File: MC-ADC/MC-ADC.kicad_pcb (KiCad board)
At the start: 2 copper layers, 160 x 100 mm, 6 parts, among them J1 Conn_Coaxial, J12 Conn_Coaxial, J2 Conn_Coaxial, J3 Conn_Coaxial, J4 Conn_Coaxial, J5 Conn_Coaxial

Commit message: ADC Work + Start Layout
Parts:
- removed J12, J5: Conn_Coaxial, Connector_Coaxial:BNC_Amphenol_031-6575_Horizontal
- added C10: 4.7 uF, Capacitor_SMD:C_1210_3225Metric, F.Cu at (134.4, 67.3)
- added C11: 2.2 uF, Capacitor_SMD:C_1210_3225Metric, F.Cu at (123.9, 126.7)
- added C12: unpopulated, Capacitor_SMD:C_1210_3225Metric, F.Cu at (128.1, 126.7)
- added C13: unpopulated, Capacitor_SMD:C_1210_3225Metric, F.Cu at (137.1, 126.9)
- added C14: 0.1 uF, Capacitor_SMD:C_1210_3225Metric, F.Cu at (96.3, 56.6)
- added C15: 0.1 uF, Capacitor_SMD:C_1210_3225Metric, F.Cu at (96.4, 62.4)
- added C16: 10 uF, Capacitor_SMD:C_1210_3225Metric, F.Cu at (109.4, 58.0)
- added C17: 0.1 uF, Capacitor_SMD:C_1210_3225Metric, F.Cu at (109.4, 61.6)
- added C18: unpopulated, Capacitor_SMD:C_1210_3225Metric, F.Cu at (143.1, 64.3)
- added C20: 1pF, Capacitor_SMD:C_0603_1608Metric, F.Cu at (111.2, 88.2)
- added C30: 1pF, Capacitor_SMD:C_0603_1608Metric, F.Cu at (111.0, 99.9)
- added C40: 1pF, Capacitor_SMD:C_0603_1608Metric, F.Cu at (113.5, 114.3)
- added C80: 43 nF, Capacitor_SMD:C_0805_2012Metric, F.Cu at (125.2, 83.4)
- added C81: 470 pF, Capacitor_SMD:C_1206_3216Metric, F.Cu at (125.6, 87.3)
- added C82: 470 pF, Capacitor_SMD:C_1206_3216Metric, F.Cu at (139.1, 92.2)
- added C83: 470 pF, Capacitor_SMD:C_1206_3216Metric, F.Cu at (125.6, 98.1)
- added C84: 43 nF, Capacitor_SMD:C_0805_2012Metric, F.Cu at (124.9, 101.9)
- added C85: 43 nF, Capacitor_SMD:C_0805_2012Metric, F.Cu at (138.8, 95.9)
- added D20: D_Schottky, Package_TO_SOT_SMD:SOT-23, F.Cu at (184.6, 72.1)
- added D21: D_Schottky, Package_TO_SOT_SMD:SOT-23, F.Cu at (184.6, 64.6)
- added D30: D_Schottky, Package_TO_SOT_SMD:SOT-23, F.Cu at (184.0, 100.8)
- added D31: D_Schottky, Package_TO_SOT_SMD:SOT-23, F.Cu at (184.0, 93.3)
- added D41: D_Schottky, Package_TO_SOT_SMD:SOT-23, F.Cu at (185.0, 129.0)
- added D42: D_Schottky, Package_TO_SOT_SMD:SOT-23, F.Cu at (185.0, 121.5)
- added JP1: Jumper, Connector_PinHeader_2.54mm:PinHeader_1x03_P2.54mm_Vertical, F.Cu at (207.9, 70.7)
- added JP2: Jumper, Connector_PinHeader_2.54mm:PinHeader_1x03_P2.54mm_Vertical, F.Cu at (207.6, 98.7)
- added JP3: Jumper, Connector_PinHeader_2.54mm:PinHeader_1x03_P2.54mm_Vertical, F.Cu at (207.9, 127.2)
- added L10: 3.9 uH, Inductor_SMD:L_1812_4532Metric_Pad1.30x3.40mm_HandSolder, F.Cu at (129.8, 67.2)
- added L11: 10uH, Footprints_MC-ADC:INDPM4040X190N, F.Cu at (117.7, 127.0)
- added R10: 1.87K, Resistor_SMD:R_0603_1608Metric, F.Cu at (107.0, 64.6)
- added R11: 1.43K, Resistor_SMD:R_0603_1608Metric, F.Cu at (110.6, 64.7)
- added R12: 30.9K, Resistor_SMD:R_1206_3216Metric, F.Cu at (132.7, 126.7)
- added R13: 1.07K, Resistor_SMD:R_1206_3216Metric, F.Cu at (130.4, 120.5)
- added R20: 250R, Resistor_SMD:R_0603_1608Metric, F.Cu at (108.5, 82.5)
- added R21: 1K, Resistor_SMD:R_0603_1608Metric, F.Cu at (160.6, 64.5)
- added R22: 100R, Resistor_SMD:R_0603_1608Metric, F.Cu at (160.6, 69.9)
- added R23: 1M, Resistor_SMD:R_1206_3216Metric, F.Cu at (202.2, 70.6)
- added R24: 50R, Resistor_SMD:R_0603_1608Metric, F.Cu at (202.2, 65.3)
- added R25: 10K, Resistor_SMD:R_1206_3216Metric, F.Cu at (193.2, 68.0)
- added R26: DNP, Resistor_SMD:R_1206_3216Metric, F.Cu at (204.6, 77.3)
- added R30: 250R, Resistor_SMD:R_0603_1608Metric, F.Cu at (108.9, 94.6)
- added R31: 100R, Resistor_SMD:R_0603_1608Metric, F.Cu at (159.7, 99.0)
- added R32: 1K, Resistor_SMD:R_0603_1608Metric, F.Cu at (159.6, 94.0)
- added R33: 1M, Resistor_SMD:R_1206_3216Metric, F.Cu at (202.0, 98.8)
- added R34: 50R, Resistor_SMD:R_0603_1608Metric, F.Cu at (201.9, 93.5)
- added R35: 10K, Resistor_SMD:R_1206_3216Metric, F.Cu at (192.8, 96.6)
- added R36: DNP, Resistor_SMD:R_1206_3216Metric, F.Cu at (204.4, 105.4)
- added R40: 250R, Resistor_SMD:R_0603_1608Metric, F.Cu at (111.0, 108.8)
- added R41: 100R, Resistor_SMD:R_0603_1608Metric, F.Cu at (160.2, 127.2)
- added R42: 1K, Resistor_SMD:R_0603_1608Metric, F.Cu at (160.0, 122.2)
- added R43: 1M, Resistor_SMD:R_1206_3216Metric, F.Cu at (201.9, 126.9)
- added R44: 50R, Resistor_SMD:R_0603_1608Metric, F.Cu at (201.9, 121.8)
- added R45: 10K, Resistor_SMD:R_1206_3216Metric, F.Cu at (193.2, 124.2)
- added R46: DNP, Resistor_SMD:R_1206_3216Metric, F.Cu at (204.5, 133.9)
- added R80: 2.2K, Resistor_SMD:R_1206_3216Metric, F.Cu at (131.2, 86.0)
- added R81: 330R, Resistor_SMD:R_0603_1608Metric, F.Cu at (125.7, 91.0)
- added R82: 330R, Resistor_SMD:R_0603_1608Metric, F.Cu at (138.6, 88.2)
- added R83: 330R, Resistor_SMD:R_0603_1608Metric, F.Cu at (125.6, 94.5)
- added R84: 2.2K, Resistor_SMD:R_1206_3216Metric, F.Cu at (131.2, 98.2)
- added R85: 2.2K, Resistor_SMD:R_1206_3216Metric, F.Cu at (139.3, 98.6)
- added R86: 10K, Resistor_SMD:R_1206_3216Metric, F.Cu at (80.5, 60.5)
- added U10: MAX6126AASA30+, Package_SO:SOIC-8_3.9x4.9mm_P1.27mm, F.Cu at (102.6, 59.9)
- added U11: R-78E3.3-0.5, Package_SIP:SIP3_11.6x8.5mm, F.Cu at (131.7, 60.4)
- added U12: RD-2412D_P, Footprints_MC-ADC:RD-2412D, F.Cu at (123.0, 126.0)
- added U81: LM324DTBR2G, Footprints_MC-ADC:LM324DTBR2G, F.Cu at (172.3, 96.9)
- added U82: LT6238CGN#PBF, Package_SO:SSOP-16_3.9x4.9mm_P0.635mm, F.Cu at (132.2, 93.2)
- J1: value Conn_Coaxial -> 86094327313755E1LF; footprint Connector_Coaxial:BNC_Amphenol_031-6575_Horizontal -> Footprints_MC-ADC:86094327313755E1LF
- J2, J3, J4: footprint Connector_Coaxial:BNC_Amphenol_031-6575_Horizontal -> Footprints_MC-ADC:516345131
- moved J1 153.3 mm to (69.4, 86.2), turned to 90 degrees
- moved J3 69.1 mm to (232.5, 124.3), turned to 0 degrees
- moved J2 26.3 mm to (232.5, 96.3), turned to 0 degrees
- moved J4 19.7 mm to (232.5, 68.3), turned to 0 degrees
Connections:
- J1 pad 1: Net-(J1-Pad1) -> 24V
- J1 pad 2: Net-(J1-Pad2) -> 24V
- J1 pad 3: (no net) -> GND1
- J1 pad 4: (no net) -> GND1
- J2 pad 2: Net-(J2-Pad2) -> GND1
- J3 pad 2: Net-(J3-Pad2) -> GND1
- J4 pad 2: Net-(J4-Pad2) -> GND1

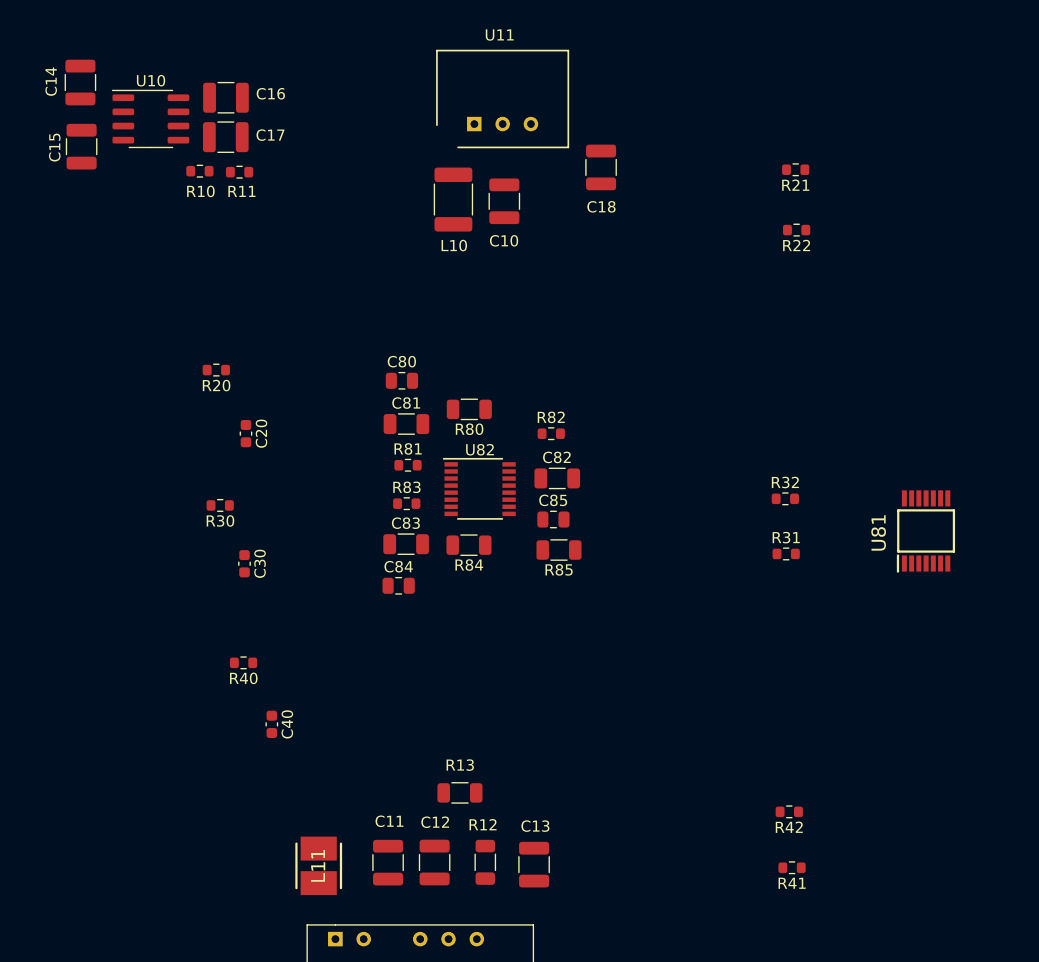
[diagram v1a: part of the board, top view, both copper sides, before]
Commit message: ADC Work + Layout
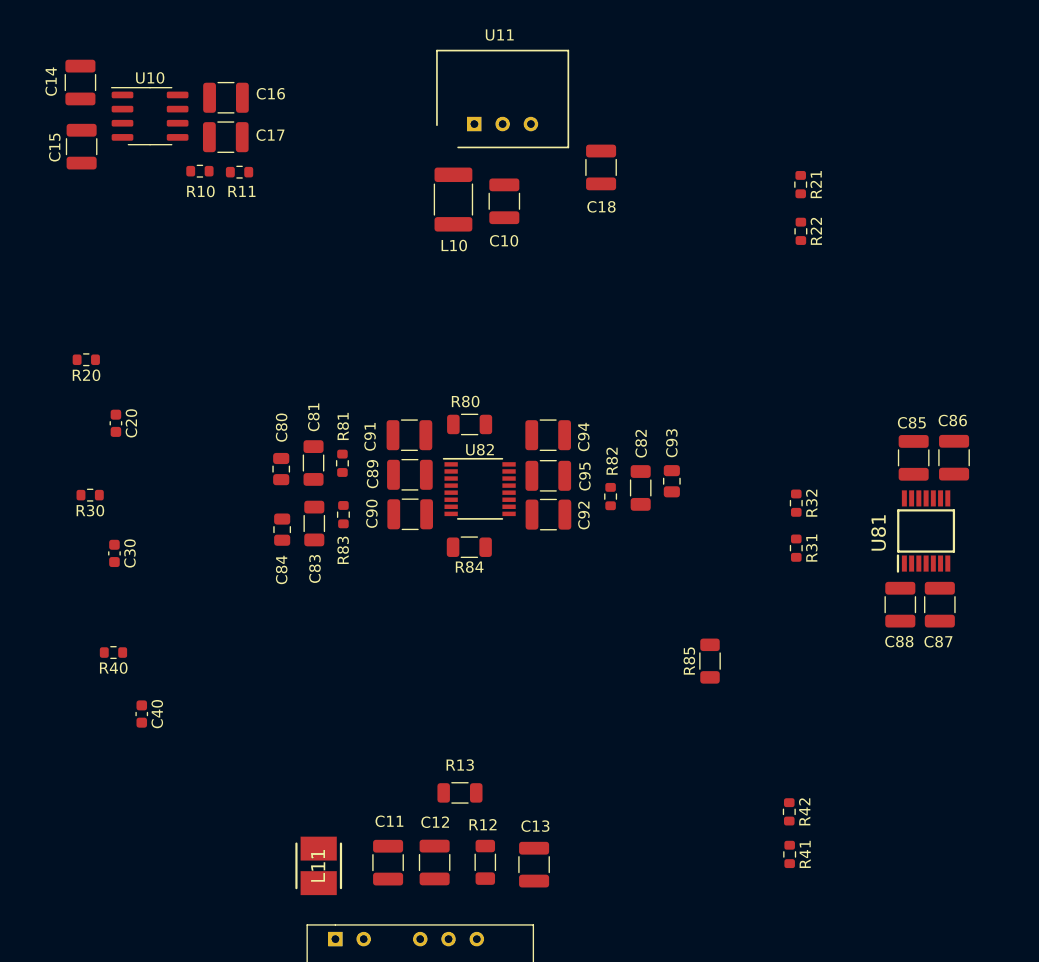
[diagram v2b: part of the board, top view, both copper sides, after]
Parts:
- added C85: 10 uF, Capacitor_SMD:C_1210_3225Metric, F.Cu at (171.1, 90.4)
- added C86: 0.1 uF, Capacitor_SMD:C_1210_3225Metric, F.Cu at (174.8, 90.3)
- added C87: 10 uF, Capacitor_SMD:C_1210_3225Metric, F.Cu at (173.5, 103.5)
- added C88: 0.1 uF, Capacitor_SMD:C_1210_3225Metric, F.Cu at (169.9, 103.5)
- added C89: 10 uF, Capacitor_SMD:C_1210_3225Metric, F.Cu at (125.9, 91.9)
- added C90: 0.1 uF, Capacitor_SMD:C_1210_3225Metric, F.Cu at (125.9, 95.4)
- added C91: 10 uF, Capacitor_SMD:C_1210_3225Metric, F.Cu at (125.9, 88.3)
- added C92: 0.1 uF, Capacitor_SMD:C_1210_3225Metric, F.Cu at (138.3, 95.5)
- added C94: 0.1 uF, Capacitor_SMD:C_1210_3225Metric, F.Cu at (138.3, 88.3)
- added C95: 10 uF, Capacitor_SMD:C_1210_3225Metric, F.Cu at (138.3, 92.0)
- moved R85 16.8 mm to (152.9, 108.6), turned to 90 degrees
- moved C80 13.4 mm to (114.3, 91.4), turned to 90 degrees
- moved R20 11.7 mm to (96.8, 81.5)
- moved R30 11.7 mm to (97.2, 93.7)
- moved R40 11.7 mm to (99.3, 107.8)
- moved C20 11.7 mm to (99.5, 87.3)
- moved C40 11.7 mm to (101.8, 113.4)
- moved C30 11.7 mm to (99.4, 98.9)
- moved C84 11.6 mm to (114.4, 96.8), turned to 90 degrees
- moved C93 11.2 mm to (149.4, 92.5), turned to 270 degrees
- moved C81 9.05 mm to (117.2, 90.8), turned to 90 degrees
- moved C83 8.45 mm to (117.3, 96.3), turned to 270 degrees
- moved R82 7.77 mm to (143.9, 93.8), turned to 270 degrees
- moved C82 7.54 mm to (146.6, 93.1), turned to 270 degrees
- moved R81 5.89 mm to (119.8, 90.9), turned to 90 degrees
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- renumbered C85 to C93
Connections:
- net /BNC_Input1/+12V renamed +12V
- C12 pad 2: /BNC_Input1/-12V -> -12V
- D21 pad 2: /BNC_Input1/-12V -> -12V
- D31 pad 2: /BNC_Input1/-12V -> -12V
- D42 pad 2: /BNC_Input1/-12V -> -12V
- R12 pad 1: /BNC_Input1/-12V -> -12V
- U12 pad 4: /BNC_Input1/-12V -> -12V

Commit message: ADC work for Alpha
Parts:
- moved R86 6.04 mm to (80.7, 66.6)
- moved J1 5.00 mm to (69.4, 91.2)

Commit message: ADC LAYOUT
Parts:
- J2, J3, J4: value Conn_Coaxial -> 5-1634513-1; footprint Footprints_MC-ADC:516345131 -> adc:516345131
- moved C13 10.2 mm to (142.3, 135.6), turned to 0 degrees
- moved C93 6.74 mm to (145.8, 98.2)
- moved C82 6.55 mm to (142.6, 98.2)
- moved R21 6.52 mm to (163.8, 71.7), turned to 90 degrees
- moved R82 5.30 mm to (140.1, 97.5)
- moved C40 4.53 mm to (99.4, 109.5)
- moved R20 3.47 mm to (99.6, 83.6), turned to 90 degrees
- moved R30 2.44 mm to (99.4, 94.7), turned to 90 degrees
- moved C92 2.27 mm to (139.4, 93.4)
- moved C94 2.27 mm to (139.4, 86.3)
- moved C95 2.27 mm to (139.4, 90.0)
- moved R35 1.90 mm to (194.2, 97.9), turned to 90 degrees
- moved R25 1.83 mm to (193.6, 69.8), turned to 90 degrees
- moved R45 1.79 mm to (193.2, 126.0), turned to 90 degrees
- moved R40 1.75 mm to (99.5, 106.1), turned to 90 degrees
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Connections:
- C93 pad 2: Net-(C93-Pad2) -> GND1
- J2 pad 3: (no net) -> GND1
- J2 pad 4: (no net) -> GND1
- J2 pad 5: (no net) -> GND1
- J3 pad 3: (no net) -> GND1
- J3 pad 4: (no net) -> GND1
- J3 pad 5: (no net) -> GND1
- J4 pad 3: (no net) -> GND1
- J4 pad 4: (no net) -> GND1
- J4 pad 5: (no net) -> GND1
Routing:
- net GND1: track 0.00 -> 56.6 mm, vias 0 -> 16
- net /BNC_Input1/BUFIN: track 0.00 -> 46.7 mm
- net /BNC_Input2/+1.3IN: track 0.00 -> 46.6 mm
- net /BNC_Input1/+1.3IN: track 0.00 -> 41.9 mm
- net +12V: track 0.00 -> 41.2 mm, vias 0 -> 4
- net Net-(J3-Pad1): track 0.00 -> 39.3 mm
- net Net-(J2-Pad1): track 0.00 -> 37.1 mm
- net Net-(J4-Pad1): track 0.00 -> 36.7 mm
- net /BNC_Input1/BUFOUT: track 0.00 -> 30.0 mm
- net /BNC_Input2/BUFIN: track 0.00 -> 23.2 mm
- net -12V: track 0.00 -> 22.3 mm, vias 0 -> 2
- net -0V4: track 0.00 -> 21.8 mm, vias 0 -> 2
- net /BNC_Input2/BUFOUT: track 0.00 -> 16.1 mm
- net /BNC_Input3/BUFIN: track 0.00 -> 14.7 mm
- net Net-(C82-Pad1): track 0.00 -> 12.6 mm
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- added copper zone on V.Cu, net +12V
- added copper zone on V.Cu, net -0V4
- added copper zone on V.Cu, net -12V
- added copper zone on GND1.Cu, net GND1
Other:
- copper layers 2 -> 4

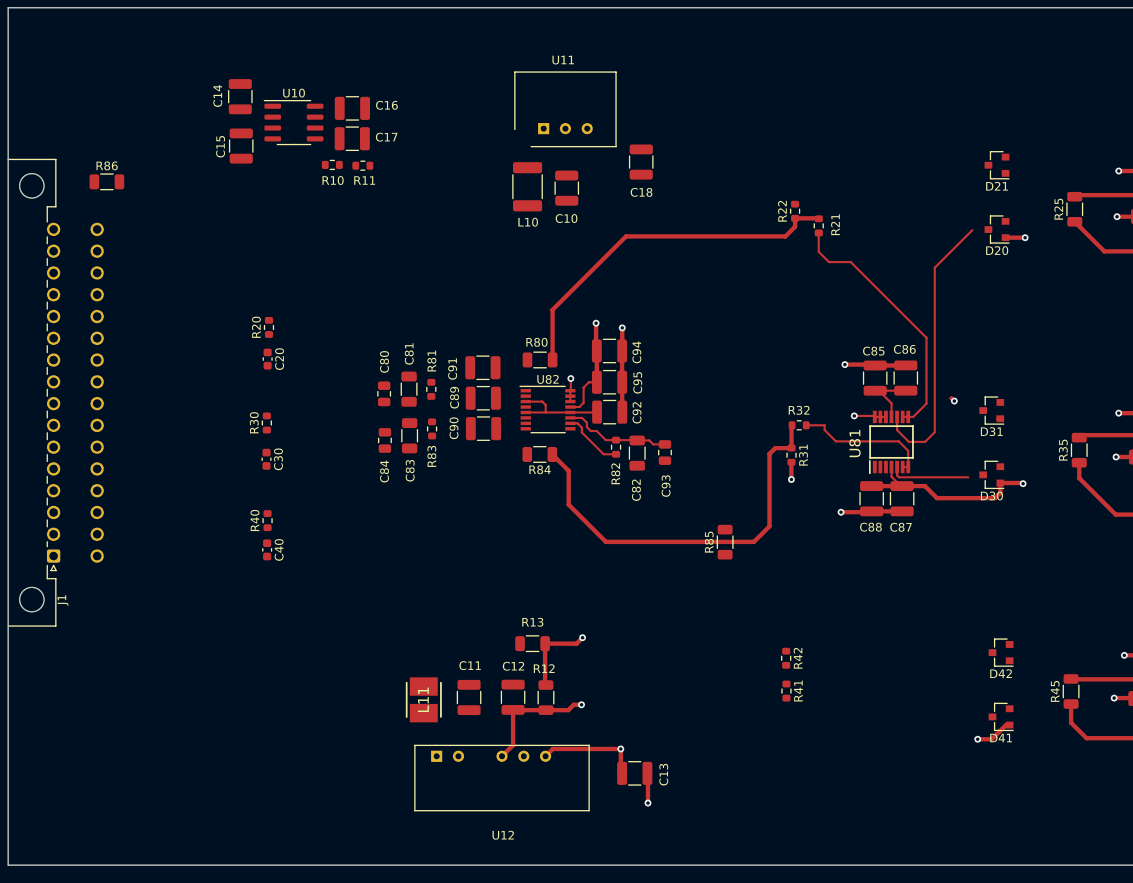
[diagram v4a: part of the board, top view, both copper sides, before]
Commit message: Prelim ADC layout complete
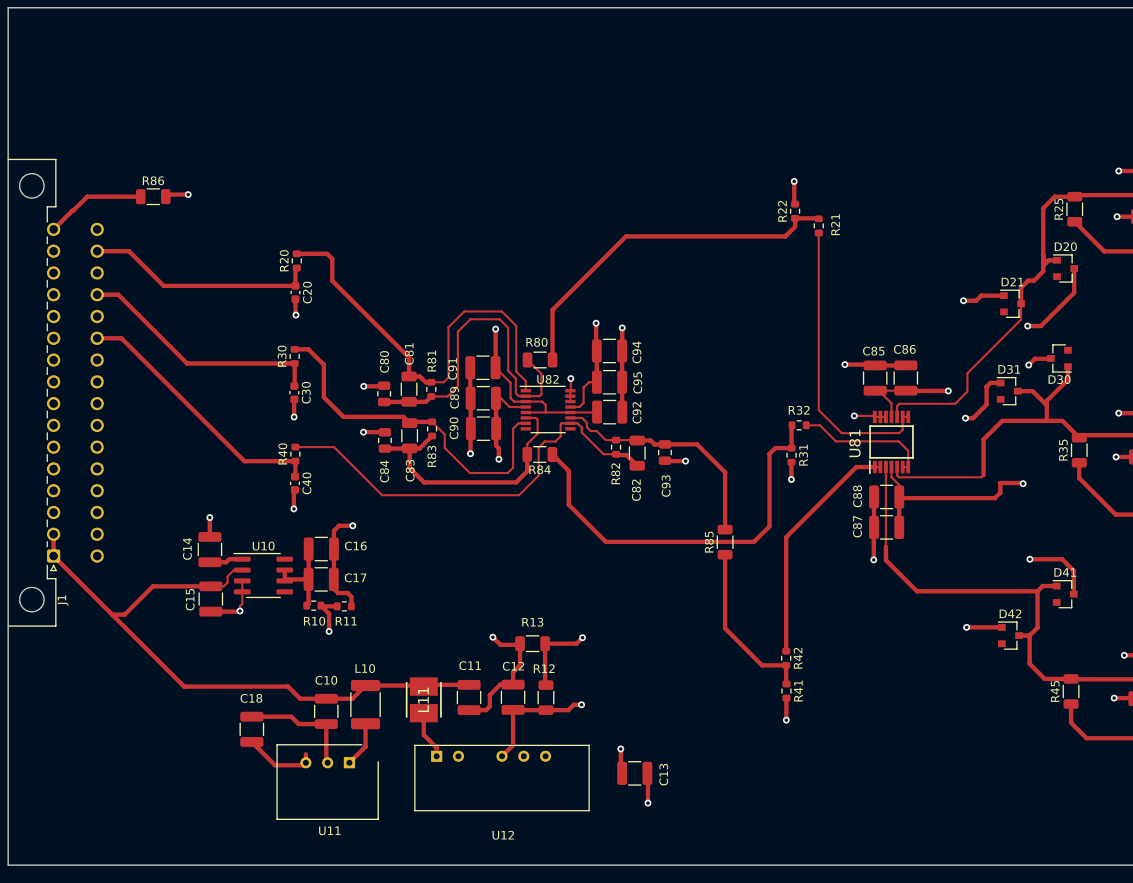
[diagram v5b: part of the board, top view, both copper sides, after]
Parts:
- D20, D21, D30, D31, D41, D42: footprint Package_TO_SOT_SMD:SOT-23 -> Footprints_MC-ADC:SOT-23
- moved C18 80.3 mm to (97.7, 130.4), turned to 90 degrees
- moved U11 77.4 mm to (109.0, 134.3), turned to 180 degrees
- moved C10 67.2 mm to (106.3, 128.4), turned to 270 degrees
- moved L10 63.3 mm to (110.9, 127.6), turned to 270 degrees
- moved C14 53.0 mm to (92.8, 109.5)
- moved C15 53.0 mm to (92.9, 115.2)
- moved U10 53.0 mm to (99.0, 112.5)
- moved C16 51.5 mm to (105.8, 109.4)
- moved C17 51.5 mm to (105.7, 113.0)
- moved R10 51.4 mm to (104.9, 116.0)
- moved R11 51.4 mm to (108.4, 116.1)
- moved D21 16.3 mm to (186.4, 80.8), turned to 0 degrees
- moved D41 16.2 mm to (192.5, 114.7), turned to 0 degrees
- moved D30 15.7 mm to (191.8, 87.2)
- moved D20 9.20 mm to (192.6, 76.7), turned to 0 degrees
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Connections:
- J1 pad 27: ADCIN1 -> ADCIN3
- J1 pad 31: ADCIN3 -> ADCIN1
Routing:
- net GND1: track 56.6 -> 137.4 mm, vias 16 -> 29
- net 24V: track 0.00 -> 76.4 mm
- net OUT_A: track 0.00 -> 50.2 mm
- net /BNC_Input3/BUFIN: track 14.7 -> 62.8 mm
- net OUT_C: track 7.15 -> 50.8 mm
- net OUT_B: track 0.00 -> 41.2 mm
- net Net-(C80-Pad1): track 0.00 -> 38.5 mm
- net Net-(C83-Pad2): track 0.00 -> 31.3 mm
- net ADCIN3: track 0.00 -> 30.9 mm
- net /BNC_Input2/BUFIN: track 23.2 -> 53.3 mm
- net ADCIN2: track 0.00 -> 29.0 mm
- net /BNC_Input3/BUFOUT: track 0.00 -> 27.7 mm
- net ADCIN1: track 0.00 -> 27.0 mm
- net 3V3: track 0.00 -> 22.4 mm, vias 0 -> 2
- net -12V: track 22.3 -> 42.9 mm, vias 2 -> 5
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- added copper zone on V.Cu, net 1.3V
- added copper zone on V.Cu, net 3V3

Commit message: ADC Gerbers Generated
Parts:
- removed R12: 30.9K, Resistor_SMD:R_1206_3216Metric
- removed R13: 1.07K, Resistor_SMD:R_1206_3216Metric
- added C19: 10uF, Capacitor_SMD:C_1210_3225Metric, F.Cu at (139.5, 121.5)
- added D11: MBR0520L, Footprints_MC-ADC:SOD3716X135N, F.Cu at (128.3, 111.3)
- added D12: MBR0520L, Footprints_MC-ADC:SOD3716X135N, F.Cu at (131.2, 118.0)
- added D13: MBR0520L, Footprints_MC-ADC:SOD3716X135N, F.Cu at (125.3, 117.9)
- added R15: 1.5K, Resistor_SMD:R_1206_3216Metric, F.Cu at (143.2, 121.5)
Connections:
- net SAFE_STATE_FLAG renamed ~SAFE_STATE_FLAG
- J1 pad 17: GND1 -> 24V
- J1 pad 2: 24V -> GND1
- J1 pad 25: GND1 -> ADCIN3
- J1 pad 27: ADCIN3 -> ADCIN2
- J1 pad 29: ADCIN2 -> ADCIN1
- J1 pad 31: ADCIN1 -> GND1
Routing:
- net GND1: track 137.4 -> 159.3 mm
- net -12V: track 42.9 -> 54.5 mm
- net -0V4: track 21.8 -> 33.1 mm
- net Net-(D11-Pad1): track 0.00 -> 5.36 mm
- net ADCIN2: track 29.0 -> 26.9 mm
- net ADCIN3: track 30.9 -> 28.8 mm
- net 24V: track 76.4 -> 78.0 mm
- net ADCIN1: track 27.0 -> 25.7 mm
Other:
- board text added: "ADC Card 1 (BNC Connectors) NCSU ECE Senior Design 2021-2022 Project 20: Modular Computer Jacob Williams, Julia Germano, Zach Murray"
